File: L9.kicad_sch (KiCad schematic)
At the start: 28 parts

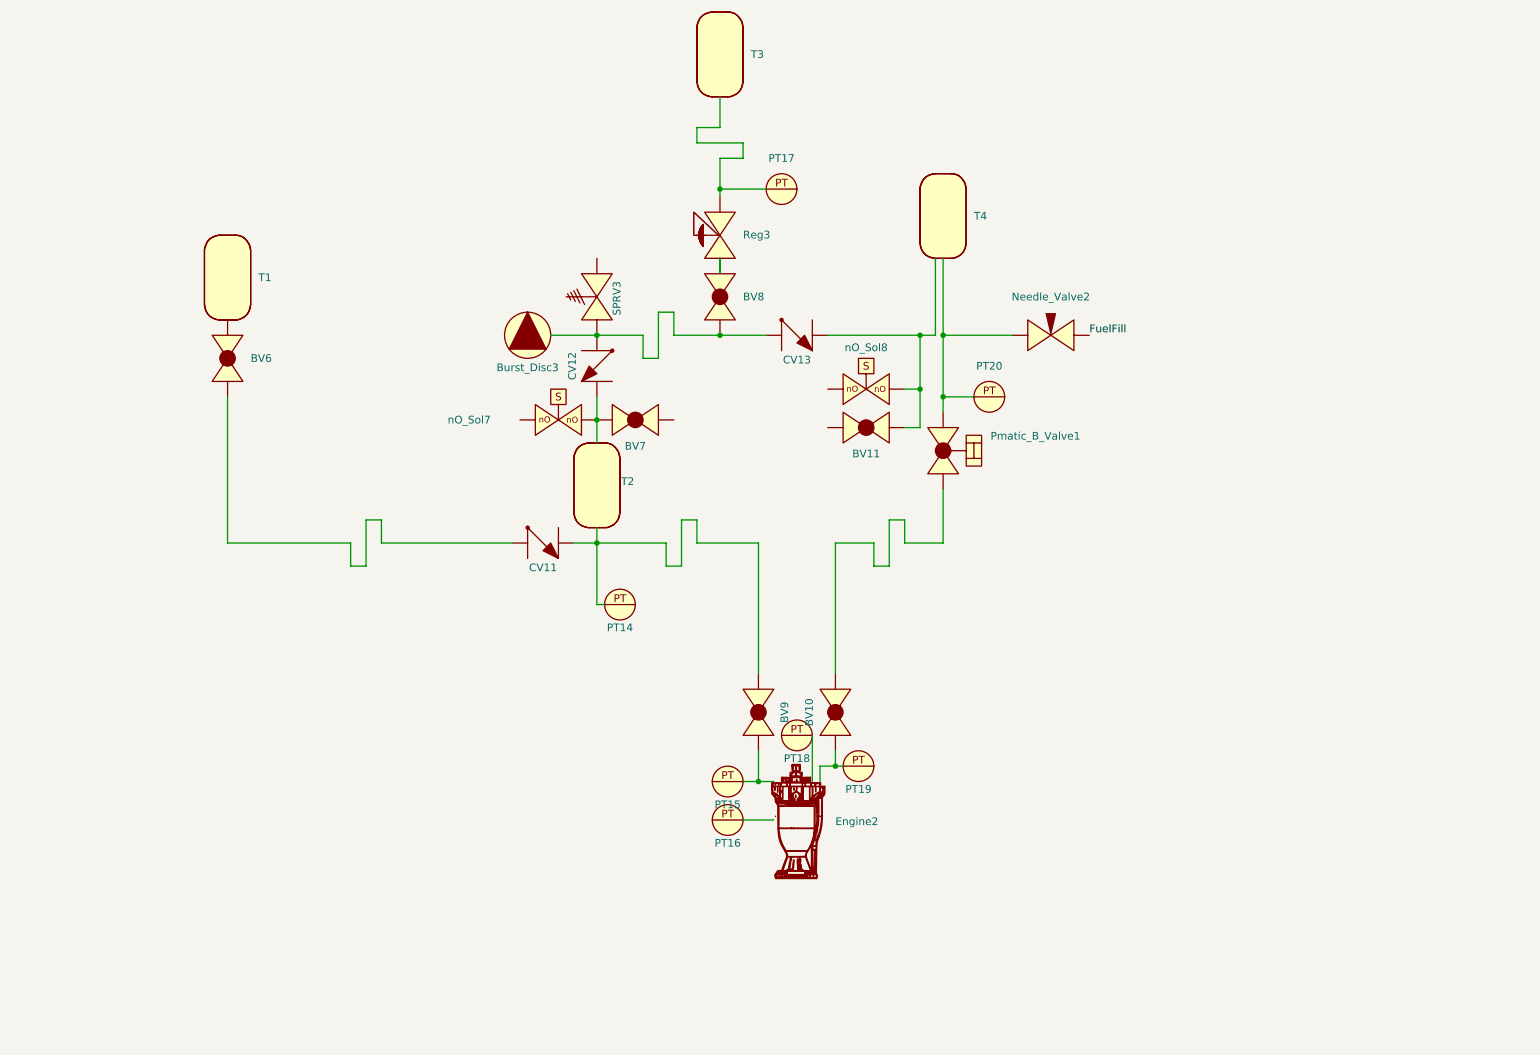
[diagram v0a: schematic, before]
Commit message: added L9 P&ID from Babs, he had problems using git
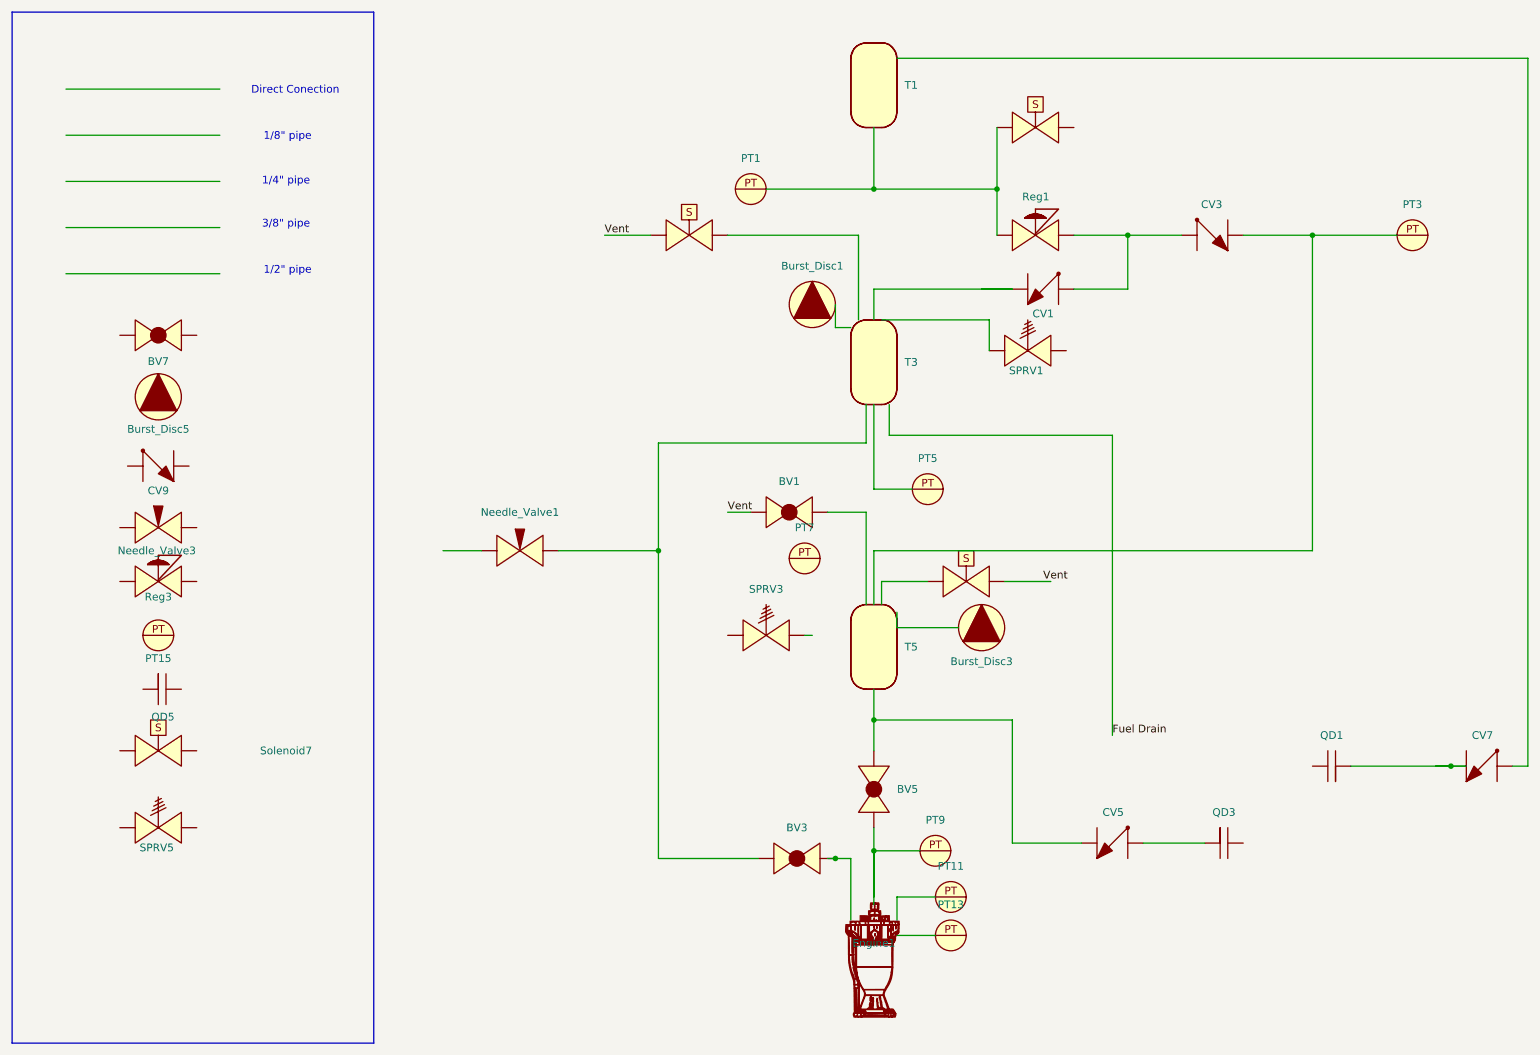
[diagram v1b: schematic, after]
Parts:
- removed BV10, BV11, BV6, BV8, BV9: (no value), symbol PID_symbols:Ball_Valve
- removed CV11, CV12, CV13: (no value), symbol PID_symbols:Check_Valve
- removed Engine2: (no value), symbol PID_symbols:Engine
- removed Needle_Valve2: (no value), symbol PID_symbols:Needle_Valve
- removed PT14, PT16, PT17, PT18, PT19, PT20: (no value), symbol PID_symbols:Pressure_Transducer
- removed Pmatic_B_Valve1: (no value), symbol PID_symbols:Pneumatic_Rotary_Ball_Valve
- removed T2, T4: (no value), symbol PID_symbols:Tank
- removed nO_Sol7, nO_Sol8: ~, symbol PID_symbols:Solenoid
- added BV1, BV3, BV5: (no value), symbol PID_symbols:Ball_Valve
- added Burst_Disc1, Burst_Disc5: (no value), symbol PID_symbols:Burst_Disc
- added CV1, CV3, CV5, CV7, CV9: (no value), symbol PID_symbols:Check_Valve
- added Engine1: (no value), symbol PID_symbols:Engine
- added Needle_Valve1, Needle_Valve3: (no value), symbol PID_symbols:Needle_Valve
- added PT1, PT11, PT13, PT3, PT5, PT7, PT9: (no value), symbol PID_symbols:Pressure_Transducer
- added QD1, QD3, QD5: (no value), symbol PID_symbols:Quick_Disconnect
- added Reg1: (no value), symbol PID_symbols:Pressure_Regulator
- added SPRV1, SPRV5: (no value), symbol PID_symbols:SPRV
- added Solenoid1, Solenoid3, Solenoid5, Solenoid7: ~, symbol PID_symbols:Solenoid
- added T5: (no value), symbol PID_symbols:Tank
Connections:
- net at SPRV3.: no longer Burst_Disc3.
- net at T3.: now also PT5.; no longer Reg3.
- new net: CV5., QD3.
- new net: CV3., PT3., T5.
- new net: CV1., CV3., Reg1.
- new net: CV1., T3.
- new net: CV7., QD1.
- new net: BV5., CV5., T5.
- new net: PT1., Reg1., Solenoid1., T1.
- new net: BV3., Engine1.
- new net: Engine1., PT11.
- new net: BV5., Engine1., PT9.
- new net: BV3., Needle_Valve1.
- new net Vent: BV1., Solenoid3., Solenoid5.
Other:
- note added: "1/2" pipe"
- note added: "1/4" pipe"
- note added: "1/8" pipe"
- note added: "3/8" pipe"
- note added: "Direct Conection"

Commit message: okokok
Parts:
- BV12: renamed from BV7; value (none) -> ~
- BV13: renamed from BV1; value (none) -> ~
- BV14: renamed from BV3; value (none) -> ~
- BV15: renamed from BV5; value (none) -> ~
- Burst_Disc4: renamed from Burst_Disc5; value (none) -> ~
- Burst_Disc5: renamed from Burst_Disc1; value (none) -> ~
- Burst_Disc6: renamed from Burst_Disc3; value (none) -> ~
- CV14: renamed from CV9; value (none) -> ~
- CV15: renamed from CV1; value (none) -> ~
- CV16: renamed from CV5; value (none) -> ~
- CV17: renamed from CV3; value (none) -> ~
- CV18: renamed from CV7; value (none) -> ~
- Engine3: renamed from Engine1; value (none) -> ~
- Needle_Valve3: value (none) -> ~
- Needle_Valve4: renamed from Needle_Valve1; value (none) -> ~
- PT21: renamed from PT15; value (none) -> ~
- PT22: renamed from PT1; value (none) -> ~
- PT23: renamed from PT7; value (none) -> ~
- PT24: renamed from PT5; value (none) -> ~
- PT25: renamed from PT9; value (none) -> ~
- PT26: renamed from PT11; value (none) -> ~
- PT27: renamed from PT13; value (none) -> ~
- PT28: renamed from PT3; value (none) -> ~
- QD4: renamed from QD5; value (none) -> ~
- QD5: renamed from QD3; value (none) -> ~
- QD6: renamed from QD1; value (none) -> ~
- Reg4: renamed from Reg3; value (none) -> ~
- Reg5: renamed from Reg1; value (none) -> ~
- SPRV4: renamed from SPRV5; value (none) -> ~
- SPRV5: renamed from SPRV3; value (none) -> ~
- SPRV6: renamed from SPRV1; value (none) -> ~
- T10: renamed from T3; value (none) -> ~
- T11: renamed from T5; value (none) -> ~
- T9: renamed from T1; value (none) -> ~
- renumbered Solenoid7 to Solenoid1, Solenoid3 to Solenoid2, Solenoid5 to Solenoid3, Solenoid1 to Solenoid4
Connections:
- net at QD5.: now also CV16.
- net at CV16.: now also BV15., T11.; no longer QD5.
- net at PT28.: now also CV17., T11.
- net at CV18.: now also QD6.
- net at QD6.: no longer CV18.
- net at Engine3.: now also BV15., PT25.; no longer BV14.
- net at PT26.: no longer Engine3.
- net at Needle_Valve4.: now also BV14.
- new net: CV15., CV17., Reg5.
- new net: PT22., Reg5., Solenoid4., T9.
- new net: BV14., Engine3.
- new net: Engine3., PT26.
- now unconnected: PT22., PT25., Solenoid4., T9.
